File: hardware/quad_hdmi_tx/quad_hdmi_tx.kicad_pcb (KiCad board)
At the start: 4 copper layers, 115 x 110 mm, 143 parts, among them J1 HDMI_A, J2 HDMI_A, J3 HDMI_A, J4 HDMI_A, J5 USB-C 5V in, J6 5V ALT IN, J7 FPGA_J7, J8 FPGA_J8, U11 ADV7513BSWZ, U12 TPD12S016PWR, U13 TLV1117LV18DCYR, U21 ADV7513BSWZ, U22 TPD12S016PWR, U23 TLV1117LV18DCYR, U31 ADV7513BSWZ, U32 TPD12S016PWR, U33 TLV1117LV18DCYR, U41 ADV7513BSWZ, U42 TPD12S016PWR, U43 TLV1117LV18DCYR, U5 AP63203WU

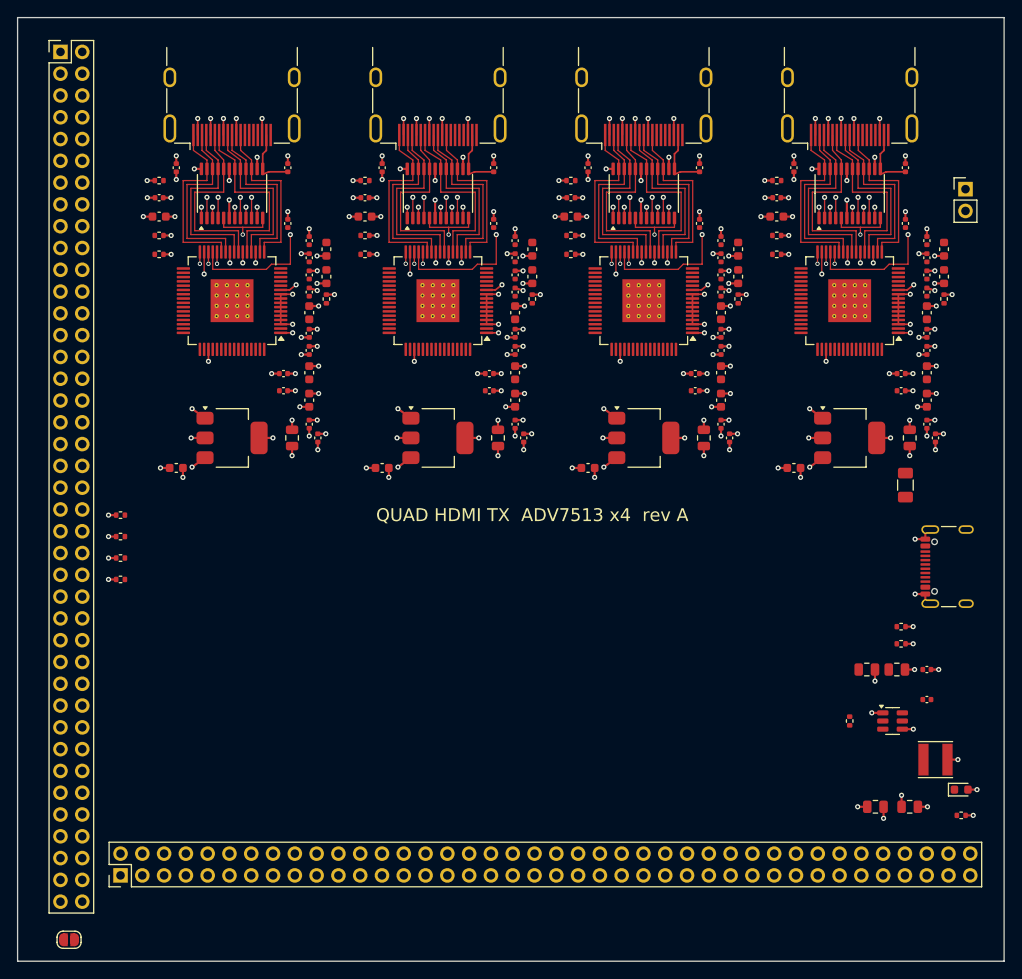
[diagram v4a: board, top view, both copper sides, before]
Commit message: 基板レイアウト完了: DRC 未接続 0 / クリアランス違反 0、ガーバー・ドリル・CPL を出力
- FreeRouting 1.9 (16 パス) の結果を取り込み、ADV pin15 (AVDD) の残り 2 本をスクリプトで接続
- 外層 GND ベタ、未使用アクセスビアの削除、DRC レポート
- fab/: ガーバー (4 層 + マスク/ペースト/シルク/外形)、Excellon ドリル、CPL、各層 PDF
- README にレイアウト結果 (層画像、ネット長、TMDS ペア長差) と発注前チェックリストを追記

Co-Authored-By: Claude Fable 5.1 <noreply@anthropic.com>
Claude-Session: https://claude.ai/code/session_01JGo25NCpKCcdkj7JC5mDdQ
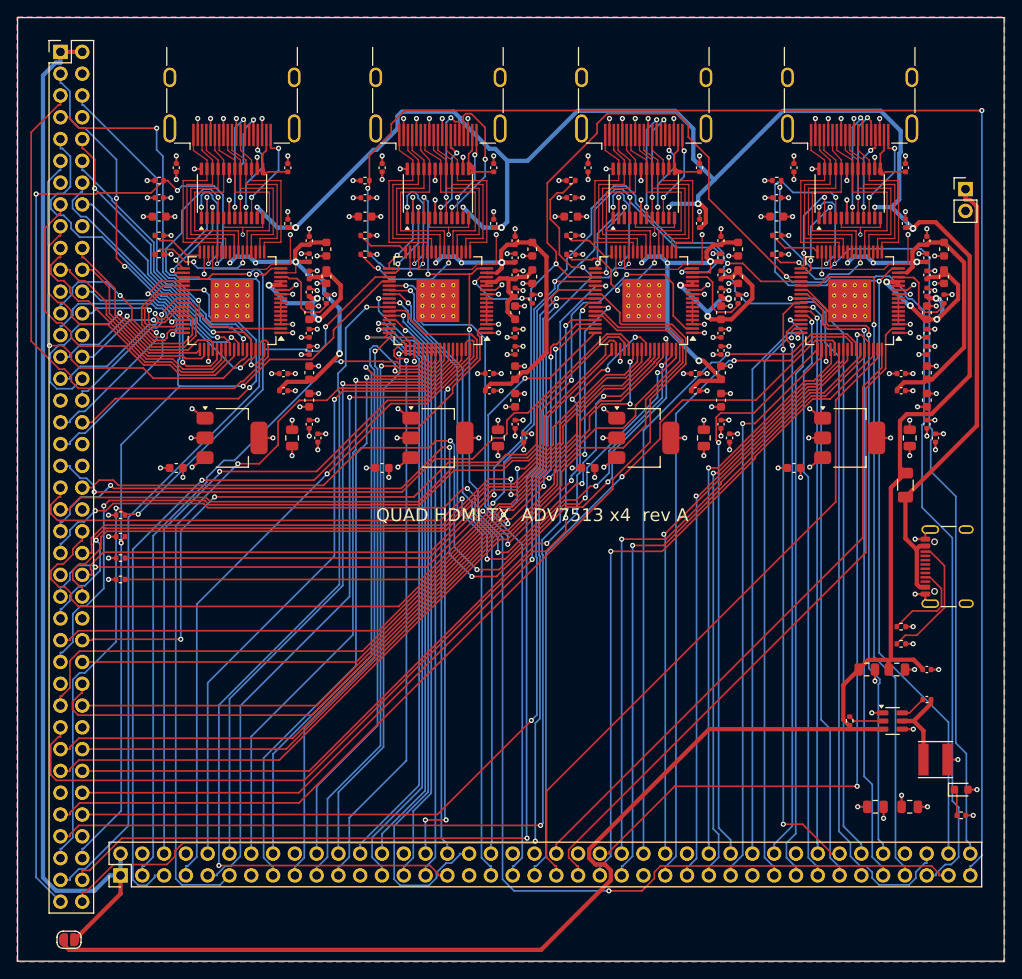
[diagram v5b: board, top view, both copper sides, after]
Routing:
- net +5V: track 5.05 -> 336.5 mm, vias 4 -> 8
- net I2C_B_SCL: track 0.00 -> 225.0 mm, vias 0 -> 3
- net I2C_B_SDA: track 0.00 -> 215.3 mm, vias 0 -> 3
- net CH2_INT: track 1.38 -> 184.2 mm, vias 1 -> 3
- net CH3_HPD: track 2.41 -> 159.6 mm, vias 1 -> 3
- net CH3_INT: track 1.38 -> 147.5 mm, vias 1 -> 3
- net CH2_HPD: track 2.41 -> 145.6 mm, vias 1 -> 4
- net CH3_D23: track 0.00 -> 124.6 mm, vias 0 -> 2
- net FPGA_5V: track 0.00 -> 122.6 mm
- net CH1_INT: track 1.38 -> 116.9 mm, vias 1 -> 3
- net CH3_D21: track 0.00 -> 114.7 mm
- net CH3_D22: track 0.00 -> 113.2 mm, vias 0 -> 2
- net I2C_A_SCL: track 0.00 -> 110.6 mm, vias 0 -> 4
- net CH1_HPD: track 2.41 -> 111.4 mm, vias 1 -> 2
- net I2C_A_SDA: track 0.00 -> 108.5 mm, vias 0 -> 3
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- added copper zone on B.Cu, net GND
- added copper zone on F.Cu, net GND

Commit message: レイアウト修正: HDMI/USB-C を基板端に合わせて再配線、DRC 未接続 0 / クリアランス違反 0
- gen_pcb.py: フットプリントの "PCB Edge" 線が外形に一致するよう J1-J4 (y=7.02) と J5 (x=111.33) を移動
- gen_pcb.py: ADV DVDD_3V (pin29) を B.Cu 経由で島の外へ (右上コーナー経由が HPD pin16 を塞いでいた)
- route_pcb.py: 未接続の島を最寄り端点間で L 字/直線/ビア経由で接続する DRC ゲート付きフィクサ、片層ビアの削除
- render_images.py: fab/*.pdf から docs/images/pcb-*.png を生成
- ガーバー・ドリル・CPL・PDF を再出力、README の検証状況とチェックリスト (コネクタのはみ出し) を更新

Co-Authored-By: Claude Fable 5.1 <noreply@anthropic.com>
Claude-Session: https://claude.ai/code/session_01JGo25NCpKCcdkj7JC5mDdQ
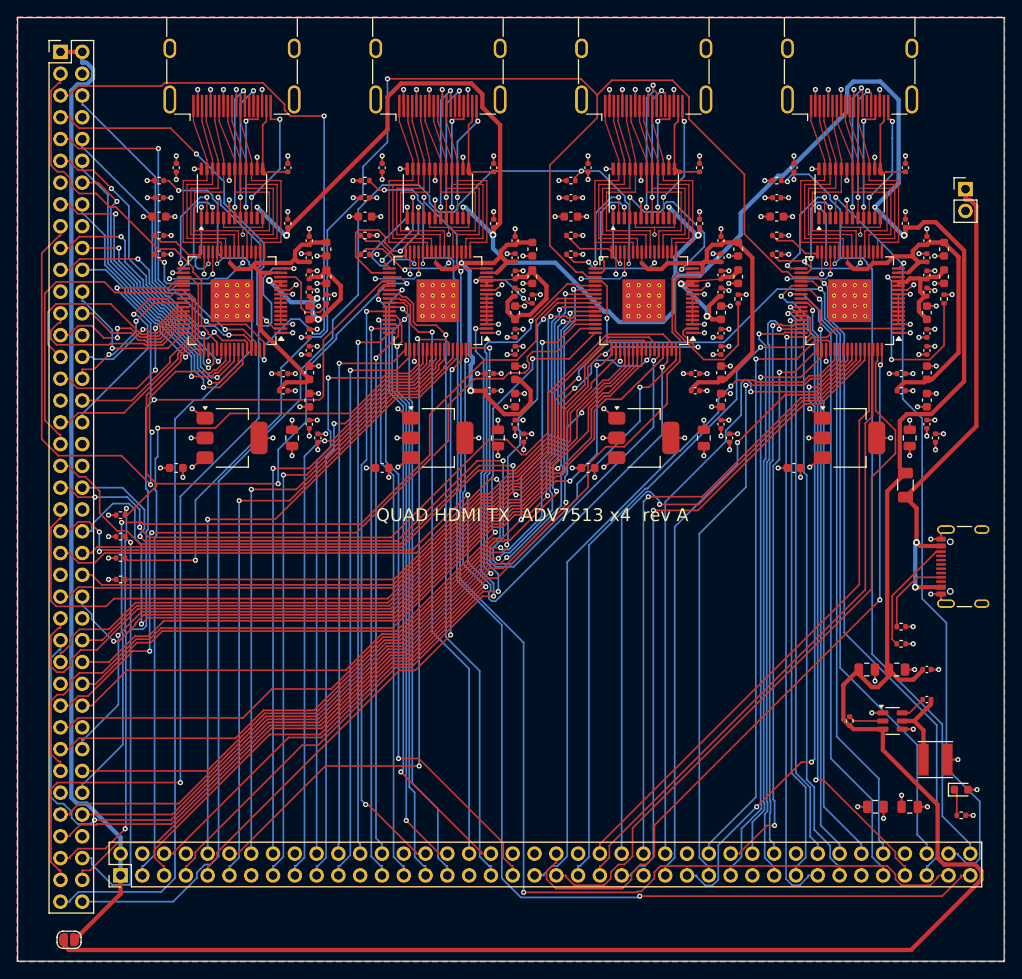
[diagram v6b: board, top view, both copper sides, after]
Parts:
- moved J1 3.38 mm to (25.0, 7.02)
- moved J2 3.38 mm to (49.0, 7.02)
- moved J3 3.38 mm to (73.0, 7.02)
- moved J4 3.38 mm to (97.0, 7.02)
- moved J5 1.83 mm to (111.3, 64.0)
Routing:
- net +5V: track 336.5 -> 388.3 mm
- net I2C_B_SDA: track 215.3 -> 179.7 mm
- net CH2_INT: track 184.2 -> 150.8 mm
- net CH3_D8: track 85.5 -> 117.8 mm, vias 2 -> 3
- net CH2_D18: track 102.2 -> 69.9 mm, vias 2 -> 1
- net CH3_HPD: track 159.6 -> 131.1 mm, vias 3 -> 2
- net I2C_A_SDA: track 108.5 -> 136.9 mm
- net CH1_D7: track 35.1 -> 63.2 mm, vias 0 -> 2
- net +3V3: track 130.8 -> 103.2 mm, vias 47 -> 51
- net I2C_B_SCL: track 225.0 -> 243.8 mm
- net CH3_D23: track 124.6 -> 106.5 mm
- net I2C_A_SCL: track 110.6 -> 128.4 mm
- net CH1_D19: track 34.4 -> 16.8 mm, vias 1 -> 2
- net CH4_D1: track 88.6 -> 71.8 mm, vias 2 -> 0
- net CH1_D22: track 39.4 -> 23.6 mm, vias 2 -> 1
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
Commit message: レイアウト rev B: 115 × 38 mm の細長い 6 層基板に再配置、ヘッダ配線を全数固定して DRC 未接続 0 / クリアランス違反 0
- 基板を HDMI 4 個分の横幅 (115 mm) × 縦 38 mm (横の 1/3) に変更、6 層 (F / GND / SIG1 / SIG2 / PWR / B)
- FPGA ヘッダ 2×40 を裏面に 2 本、長辺と平行に配置。ヘッダの列が各 ADV7513 の真下に来る
- J7/J8 のピン割り当てを配線経路に合わせて変更 (J7 = ADV 左辺の D13-23 + D1/D2/D4/D5/D10、J8 = 下辺の残り + CLK/DE/HS/VS/HPD/INT)
- RGB バス 30 本 × 4 ch、DDC/CEC/HPD、AVDD/PVDD の一部、FPGA_5V を gen_pcb.py で内層に固定配線 (交差しないレーン割り当て)
- 部品の再配置 (C01/C16/C20/R2/R4、左の 1V8 コンデンサ列を x=cx-10.3 へ)、1V8 の島の首を広げてプレーンの連続を確保
- FreeRouting 1.9 (-mp 24 -oit 1.0、約 10 分) で残りを配線: 配線 2010 本、ビア 634 個、TMDS はビアなし・ペア内長差 0.47 mm 以下
- ガーバー / ドリル / CPL / 各層 PDF と docs の画像を再生成、README と fpga_header_pinmap.csv を更新

Co-Authored-By: Claude Fable 5.1 <noreply@anthropic.com>
Claude-Session: https://claude.ai/code/session_01JGo25NCpKCcdkj7JC5mDdQ
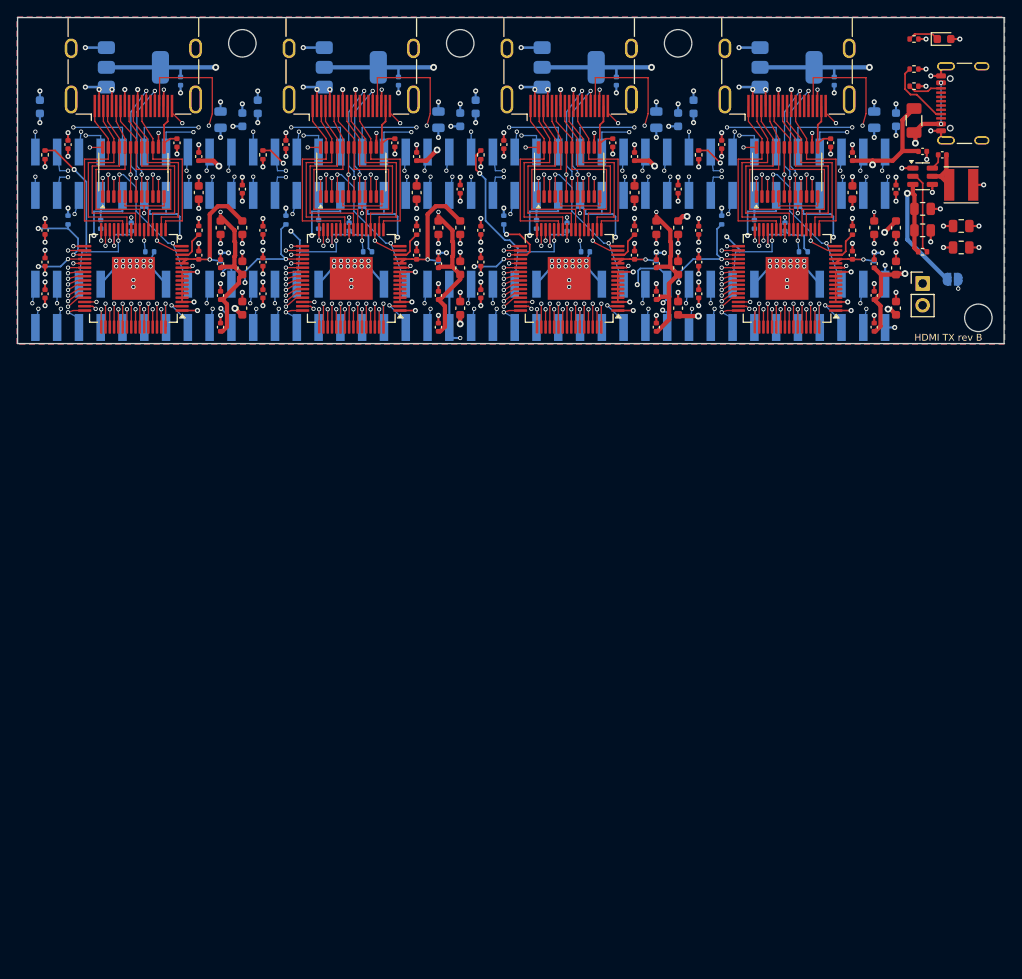
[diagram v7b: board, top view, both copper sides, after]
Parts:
- added H1: M3, MountingHole_3.2mm_M3, F.Cu at (26.2, 3.00)
- added H2: M3, MountingHole_3.2mm_M3, F.Cu at (51.6, 3.00)
- added H3: M3, MountingHole_3.2mm_M3, F.Cu at (112.0, 35.0)
- added H4: M3, MountingHole_3.2mm_M3, F.Cu at (77.0, 3.00)
- C101, C102, C107, C108, C114, C116, C201, C202, C207, C208, C214, C216, C301, C302, C307, C308, C314, C316, C401, C402, C407, C408, C414, C416, JP1, R1, R12, R14, R2, R22, R24, R3, R32, R34, R4, R42, R44, U13, U23, U33, U43: moved to B.Cu
- J7, J8: footprint PinHeader_2x40_P2.54mm_Vertical -> PinHeader_2x40_P2.54mm_Vertical_SMD; moved to B.Cu
- U11, U21, U31, U41: footprint LQFP-64-1EP_10x10mm_P0.5mm_EP5x5mm_ThermalVias -> LQFP-64-1EP_10x10mm_P0.5mm_EP5x5mm
- moved JP1 128.6 mm to (109.0, 30.5)
- moved R8 90.7 mm to (104.5, 2.50)
- moved D1 87.5 mm to (108.0, 2.50)
- moved R4 81.7 mm to (82.1, 23.6), turned to -90 degrees
- moved J8 77.3 mm to (51.6, 33.6), turned to -90 degrees
- moved C55 68.4 mm to (110.0, 24.3)
- moved L1 67.1 mm to (110.0, 19.5)
- moved C56 65.5 mm to (110.0, 26.8)
- moved R5 65.0 mm to (104.5, 6.00)
- moved R6 65.0 mm to (104.5, 8.00)
- moved U5 63.6 mm to (105.5, 18.5)
- moved C51 63.5 mm to (107.8, 16.0)
- moved C54 60.4 mm to (105.5, 15.6)
- moved R3 59.6 mm to (56.7, 23.6), turned to -90 degrees
- moved R7 55.4 mm to (105.5, 27.3), turned to 0 degrees
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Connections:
- J7 pad 1: FPGA_5V -> CH1_D18
- J7 pad 10: CH1_D1 -> GND
- J7 pad 11: CH1_D2 -> CH1_D16
- J7 pad 12: CH1_D3 -> GND
- J7 pad 13: GND -> CH1_D20
- J7 pad 14: CH1_D4 -> GND
- J7 pad 15: CH1_D5 -> CH1_D21
- J7 pad 16: CH1_D6 -> CH1_D10
- J7 pad 17: CH1_D7 -> CH1_D2
- J7 pad 18: GND -> CH1_D1
- J7 pad 19: CH1_D8 -> CH1_D5
- J7 pad 2: FPGA_5V -> CH1_D19
- J7 pad 20: CH1_D9 -> CH1_D4
- J7 pad 21: CH1_D10 -> CH2_D18
- J7 pad 22: CH1_D11 -> CH2_D19
- J7 pad 23: GND -> CH2_D23
- J7 pad 24: CH1_D12 -> CH2_D17
- J7 pad 25: CH1_D13 -> CH2_D13
- J7 pad 26: CH1_D14 -> CH2_D15
- J7 pad 27: CH1_D15 -> CH2_D14
- J7 pad 29: CH1_D16 -> CH2_D22
- J7 pad 3: CH1_CLK -> CH1_D23
- J7 pad 30: CH1_D17 -> GND
- J7 pad 31: CH1_D18 -> CH2_D16
- J7 pad 32: CH1_D19 -> GND
- J7 pad 33: GND -> CH2_D20
- J7 pad 34: CH1_D20 -> GND
- J7 pad 35: CH1_D21 -> CH2_D21
- J7 pad 36: CH1_D22 -> CH2_D10
- J7 pad 37: CH1_D23 -> CH2_D2
- J7 pad 38: GND -> CH2_D1
- J7 pad 39: CH3_CLK -> CH2_D5
- J7 pad 4: GND -> CH1_D17
- J7 pad 40: GND -> CH2_D4
- J7 pad 41: CH3_DE -> CH3_D18
- J7 pad 42: CH3_HS -> CH3_D19
- J7 pad 43: CH3_VS -> CH3_D23
- J7 pad 44: GND -> CH3_D17
- J7 pad 45: CH3_D0 -> CH3_D13
- J7 pad 46: CH3_D1 -> CH3_D15
- J7 pad 47: CH3_D2 -> CH3_D14
- J7 pad 48: CH3_D3 -> GND
- J7 pad 49: GND -> CH3_D22
- J7 pad 5: CH1_DE -> CH1_D13
- J7 pad 50: CH3_D4 -> GND
- J7 pad 51: CH3_D5 -> CH3_D16
- J7 pad 52: CH3_D6 -> GND
- J7 pad 53: CH3_D7 -> CH3_D20
- J7 pad 55: CH3_D8 -> CH3_D21
- J7 pad 56: CH3_D9 -> CH3_D10
- J7 pad 57: CH3_D10 -> CH3_D2
- J7 pad 58: CH3_D11 -> CH3_D1
- J7 pad 59: GND -> CH3_D5
- J7 pad 6: CH1_HS -> CH1_D15
- J7 pad 60: CH3_D12 -> CH3_D4
- J7 pad 61: CH3_D13 -> CH4_D18
- J7 pad 62: CH3_D14 -> CH4_D19
- J7 pad 63: CH3_D15 -> CH4_D23
- J7 pad 64: GND -> CH4_D17
- J7 pad 65: CH3_D16 -> CH4_D13
- J7 pad 66: CH3_D17 -> CH4_D15
- J7 pad 67: CH3_D18 -> CH4_D14
- J7 pad 68: CH3_D19 -> GND
- J7 pad 69: GND -> CH4_D22
- J7 pad 7: CH1_VS -> CH1_D14
- J7 pad 70: CH3_D20 -> GND
- J7 pad 71: CH3_D21 -> CH4_D16
- J7 pad 72: CH3_D22 -> GND
- J7 pad 73: CH3_D23 -> CH4_D20
- J7 pad 75: I2C_A_SCL -> CH4_D21
- J7 pad 76: I2C_A_SDA -> CH4_D10
- J7 pad 77: CH1_HPD -> CH4_D2
- J7 pad 78: CH3_HPD -> CH4_D1
- J7 pad 79: CH1_INT -> CH4_D5
- J7 pad 80: CH3_INT -> CH4_D4
- J7 pad 9: CH1_D0 -> CH1_D22
- J8 pad 1: FPGA_5V -> CH1_D6
- J8 pad 10: CH2_D1 -> CH1_D8
- J8 pad 11: CH2_D2 -> GND
- J8 pad 12: CH2_D3 -> CH1_D3
- J8 pad 14: CH2_D4 -> CH1_HS
- J8 pad 15: CH2_D5 -> CH1_HPD
- J8 pad 16: CH2_D6 -> CH1_VS
- J8 pad 17: CH2_D7 -> CH1_DE
- J8 pad 18: GND -> CH1_D0
- J8 pad 19: CH2_D8 -> I2C_A_SCL
- J8 pad 2: FPGA_5V -> CH1_D7
- J8 pad 20: CH2_D9 -> I2C_A_SDA
- J8 pad 21: CH2_D10 -> CH2_D6
- J8 pad 22: CH2_D11 -> CH2_D7
- J8 pad 23: GND -> CH2_CLK
- J8 pad 24: CH2_D12 -> CH2_D9
- J8 pad 25: CH2_D13 -> CH2_INT
- J8 pad 26: CH2_D14 -> CH2_D12
- J8 pad 27: CH2_D15 -> GND
- J8 pad 28: GND -> CH2_D11
- J8 pad 29: CH2_D16 -> GND
- J8 pad 3: CH2_CLK -> CH1_CLK
- J8 pad 30: CH2_D17 -> CH2_D8
- J8 pad 31: CH2_D18 -> GND
- J8 pad 32: CH2_D19 -> CH2_D3
- J8 pad 34: CH2_D20 -> CH2_HS
- J8 pad 35: CH2_D21 -> CH2_HPD
- J8 pad 36: CH2_D22 -> CH2_VS
- J8 pad 37: CH2_D23 -> CH2_DE
- J8 pad 38: GND -> CH2_D0
- J8 pad 39: CH4_CLK -> FPGA_5V
- J8 pad 4: GND -> CH1_D9
- J8 pad 40: GND -> FPGA_5V
- J8 pad 41: CH4_DE -> CH3_D6
- J8 pad 42: CH4_HS -> CH3_D7
- J8 pad 43: CH4_VS -> CH3_CLK
- J8 pad 44: GND -> CH3_D9
- J8 pad 45: CH4_D0 -> CH3_INT
- J8 pad 46: CH4_D1 -> CH3_D12
- J8 pad 47: CH4_D2 -> GND
- J8 pad 48: CH4_D3 -> CH3_D11
- J8 pad 5: CH2_DE -> CH1_INT
- J8 pad 50: CH4_D4 -> CH3_D8
- J8 pad 51: CH4_D5 -> GND
- J8 pad 52: CH4_D6 -> CH3_D3
- J8 pad 53: CH4_D7 -> GND
- J8 pad 54: GND -> CH3_HS
- J8 pad 55: CH4_D8 -> CH3_HPD
- J8 pad 56: CH4_D9 -> CH3_VS
- J8 pad 57: CH4_D10 -> CH3_DE
- J8 pad 58: CH4_D11 -> CH3_D0
- J8 pad 59: GND -> I2C_B_SCL
- J8 pad 6: CH2_HS -> CH1_D12
- J8 pad 60: CH4_D12 -> I2C_B_SDA
- J8 pad 61: CH4_D13 -> CH4_D6
- J8 pad 62: CH4_D14 -> CH4_D7
- J8 pad 63: CH4_D15 -> CH4_CLK
- J8 pad 64: GND -> CH4_D9
- J8 pad 65: CH4_D16 -> CH4_INT
- J8 pad 66: CH4_D17 -> CH4_D12
- J8 pad 67: CH4_D18 -> GND
- J8 pad 68: CH4_D19 -> CH4_D11
- J8 pad 7: CH2_VS -> GND
- J8 pad 70: CH4_D20 -> CH4_D8
- J8 pad 71: CH4_D21 -> GND
- J8 pad 72: CH4_D22 -> CH4_D3
- J8 pad 73: CH4_D23 -> GND
- J8 pad 74: GND -> CH4_HS
- J8 pad 75: I2C_B_SCL -> CH4_HPD
- J8 pad 76: I2C_B_SDA -> CH4_VS
- J8 pad 77: CH2_HPD -> CH4_DE
- J8 pad 78: CH4_HPD -> CH4_D0
- J8 pad 79: CH2_INT -> GND
- J8 pad 8: GND -> CH1_D11
- J8 pad 80: CH4_INT -> GND
- J8 pad 9: CH2_D0 -> GND
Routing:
- net +5V: track 388.3 -> 196.8 mm, vias 8 -> 9
- net I2C_B_SCL: track 243.8 -> 55.9 mm, vias 3 -> 5
- net GND: track 197.9 -> 325.8 mm, vias 147 -> 203
- net I2C_B_SDA: track 179.7 -> 52.8 mm, vias 3 -> 5
- net CH2_INT: track 150.8 -> 25.4 mm
- net CH2_HPD: track 144.5 -> 20.1 mm, vias 3 -> 2
- net CH3_INT: track 148.9 -> 25.0 mm
- net CH3_D8: track 117.8 -> 5.50 mm, vias 3 -> 1
- net CH3_HPD: track 131.1 -> 20.1 mm
- net CH3_VS: track 106.6 -> 4.51 mm, vias 2 -> 1
- net CH3_HS: track 106.0 -> 5.50 mm, vias 3 -> 1
- net CH1_HPD: track 116.1 -> 20.1 mm, vias 3 -> 2
- net CH3_D0: track 105.4 -> 14.3 mm, vias 4 -> 2
- net CH3_D23: track 106.5 -> 17.1 mm
- net CH1_INT: track 110.5 -> 25.1 mm
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- added copper zone on In4.Cu, net +3V3
- added copper zone on In4.Cu, net CH1_1V8
- added copper zone on In4.Cu, net CH2_1V8
- added copper zone on In4.Cu, net CH3_1V8
- added copper zone on In4.Cu, net CH4_1V8
- removed copper zone on In2.Cu, net +3V3
- removed copper zone on In2.Cu, net CH1_1V8
- removed copper zone on In2.Cu, net CH2_1V8
- removed copper zone on In2.Cu, net CH3_1V8
- removed copper zone on In2.Cu, net CH4_1V8
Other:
- board size 115 x 110 mm -> 115 x 38 mm
- copper layers 4 -> 6
- board text added: "HDMI TX rev B"
- board text removed: "QUAD HDMI TX ADV7513 x4 rev A"
